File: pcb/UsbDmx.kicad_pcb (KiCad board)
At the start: 2 copper layers, 100 x 100 mm, 112 parts, among them CON101 10PIN_ISP_AVR, CON201 XLR3_F_GROUND, CON202 XLR3_M_GROUND, J101 USB_B, J102 Barrel_Jack, Q201 BC817, Q202 BC807, Q203 BC817, U101 74LS573, U102 USBLC6-2SC6, U103 USBN9604-28M, U104 AS6C6264, U105 L7805, U106 ATMEGA8515-16AU, U201 SN75176, U202 6N137, U203 PESD5V0S2BT, U204 6N137, U205 AM2D-0505SZ, U206 SN75176, U207 PESD5V0S2BT, Y101 24MHz

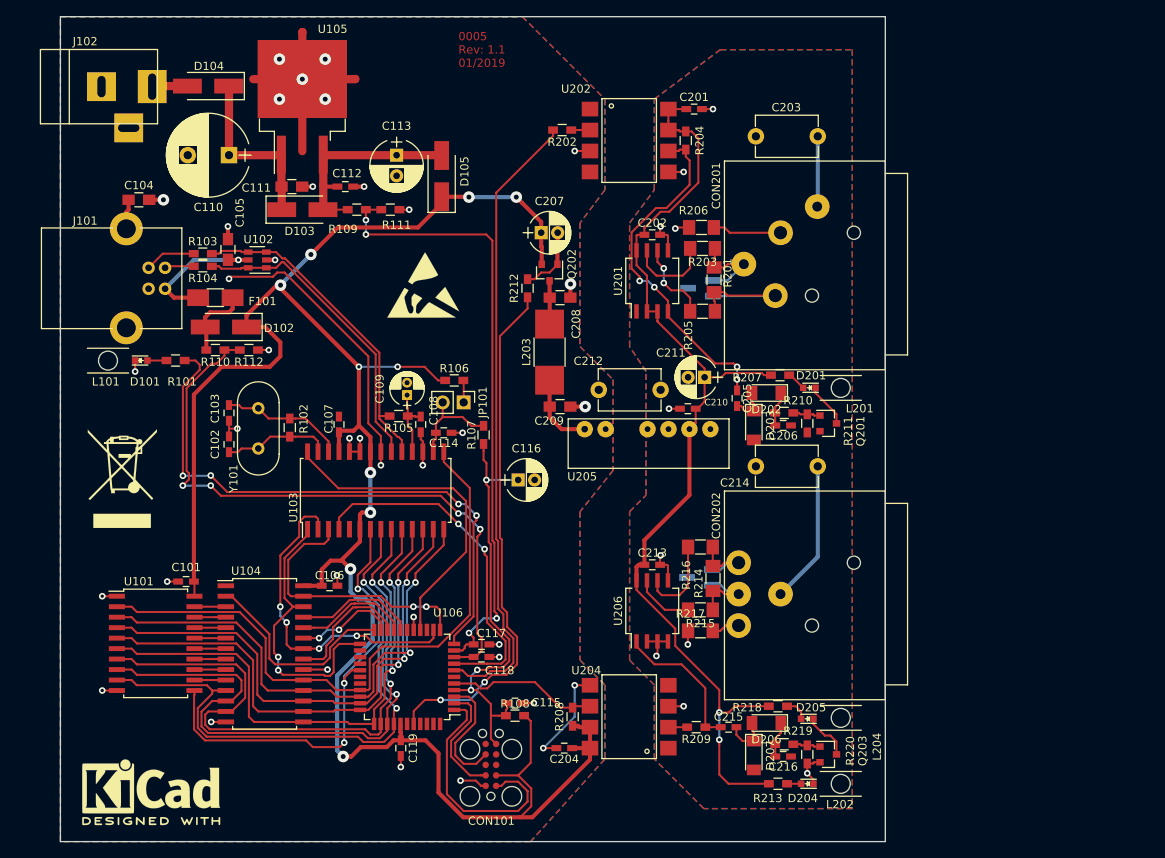
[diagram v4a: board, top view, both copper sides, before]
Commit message: changed footprints to fit better the real parts
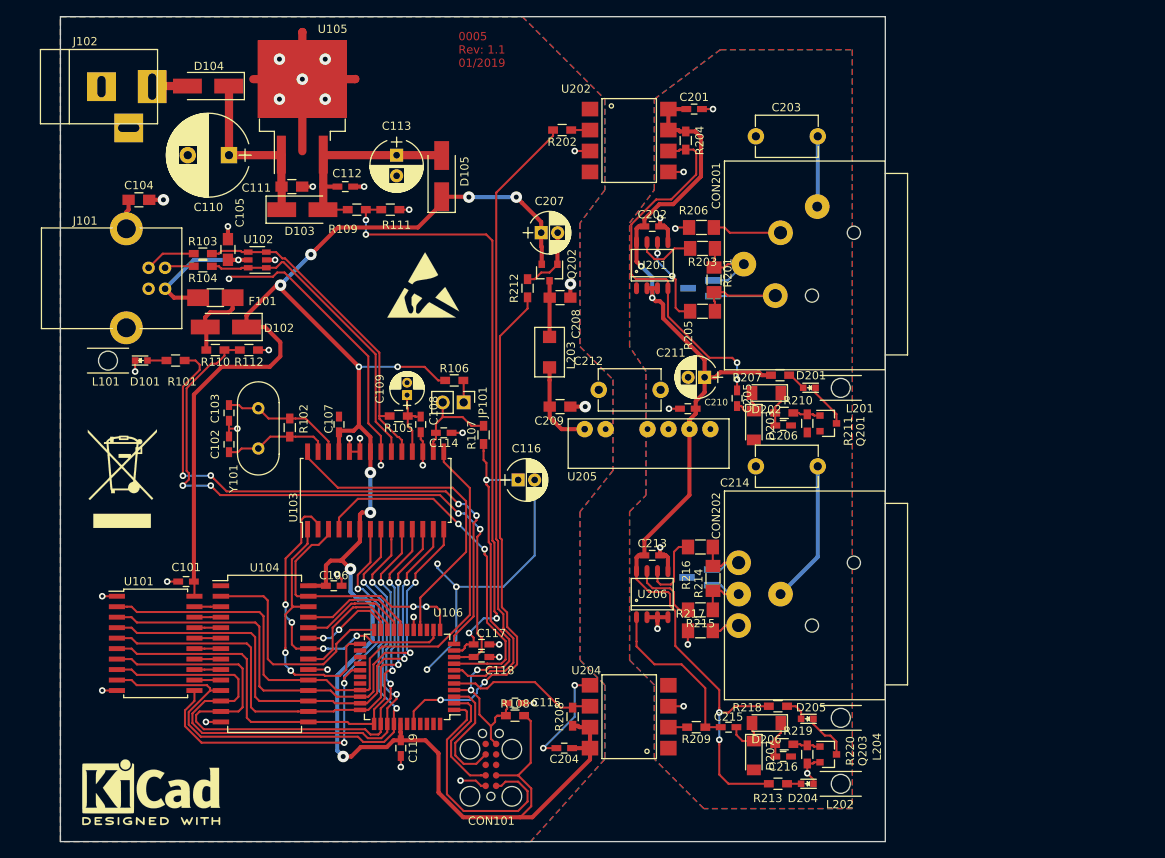
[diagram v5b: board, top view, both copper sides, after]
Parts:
- L203: footprint Resistors_SMD:R_1812_HandSoldering -> proz_choke:inductor_1812
- U104: footprint Housings_SOIC:SOIC-28W_7.5x17.9mm_Pitch1.27mm -> proz_soic:SOIC-28W_8.7x18.7mm_Pitch1.27mm
- U201, U206: footprint Housings_SOIC:SO-8_5.3x6.2mm_Pitch1.27mm -> Power_Integrations:SO-8
- moved U206 2.03 mm to (126.7, 135.0), turned to 0 degrees
- moved U201 1.91 mm to (126.7, 95.1), turned to 0 degrees
- moved C213 1.14 mm to (126.7, 130.3)
- moved C202 1.02 mm to (126.7, 90.4)
- moved C106 0.51 mm to (88.1, 134.0)
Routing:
- net GND: track 128.4 -> 163.6 mm, vias 37 -> 40
- net +5VA: track 123.6 -> 127.6 mm, vias 2 -> 4
- net Net-(C205-Pad1): track 42.5 -> 45.9 mm, vias 4 -> 2
- net /DmxInOut/TX_B: track 10.4 -> 7.30 mm
- net Net-(C215-Pad1): track 17.6 -> 20.6 mm
- net /A12: track 25.6 -> 28.4 mm
- net /A13: track 34.5 -> 31.8 mm
- net /AD2: track 75.1 -> 77.4 mm
- net /WR: track 32.9 -> 30.8 mm
- net /AD7: track 76.4 -> 78.1 mm
- net /AD1: track 75.9 -> 77.6 mm
- net /AD6: track 63.3 -> 64.9 mm
- net Net-(C209-Pad1): track 9.34 -> 10.9 mm
- net Net-(C208-Pad1): track 5.27 -> 6.82 mm
- net /AD5: track 63.0 -> 64.4 mm
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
